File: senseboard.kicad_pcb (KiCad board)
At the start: 6 copper layers, 60 x 100 mm, 81 parts, among them J1 USB_C_Receptacle_USB2.0_16P, J2 Screw_Terminal_01x02, J3 DM3AT-SF-PEJM5, J4 Conn_01x04, J5 Conn_01x08, U1 USBLC6-2SC6, U2 TPS62840DLCR, U3 TPS62840DLCR, U4 SCD41-D-R2, U5 SGP41-D-R4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

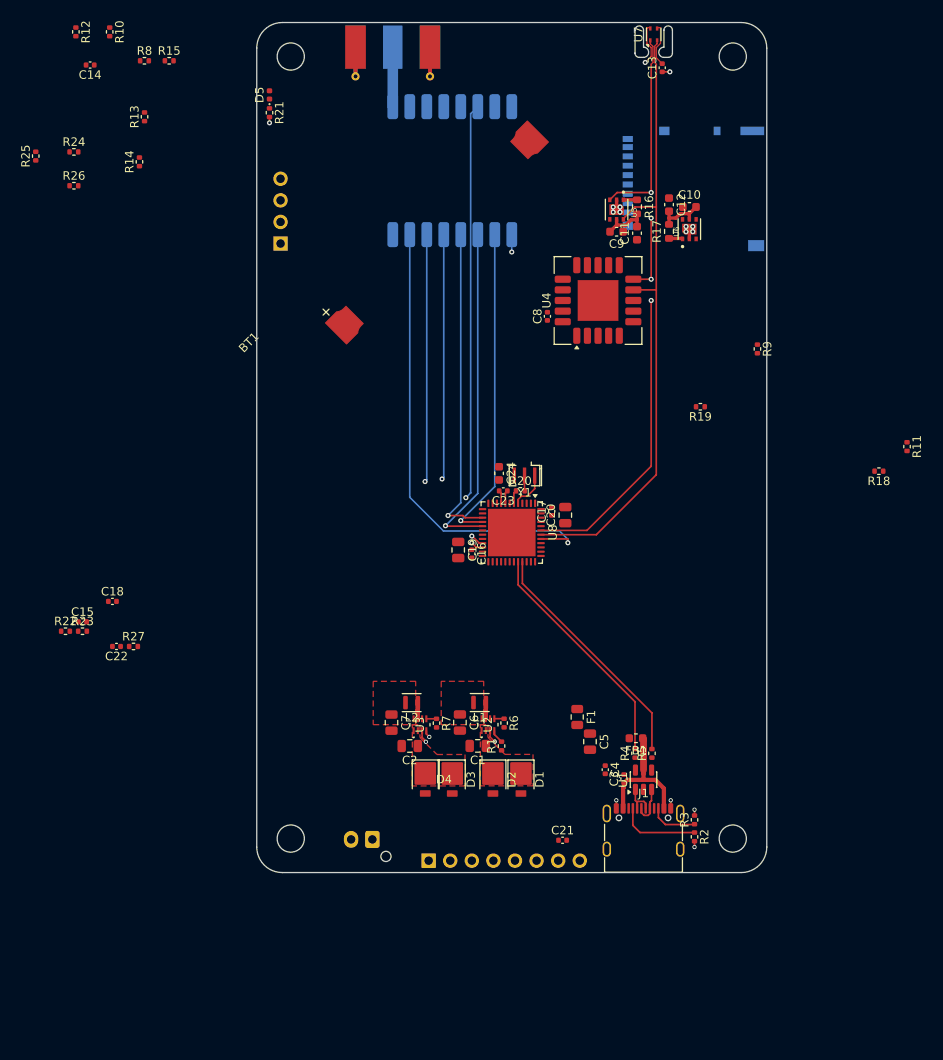
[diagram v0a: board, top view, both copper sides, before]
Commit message: added sd card protection, completed most layout, added bosch sensor, graphics
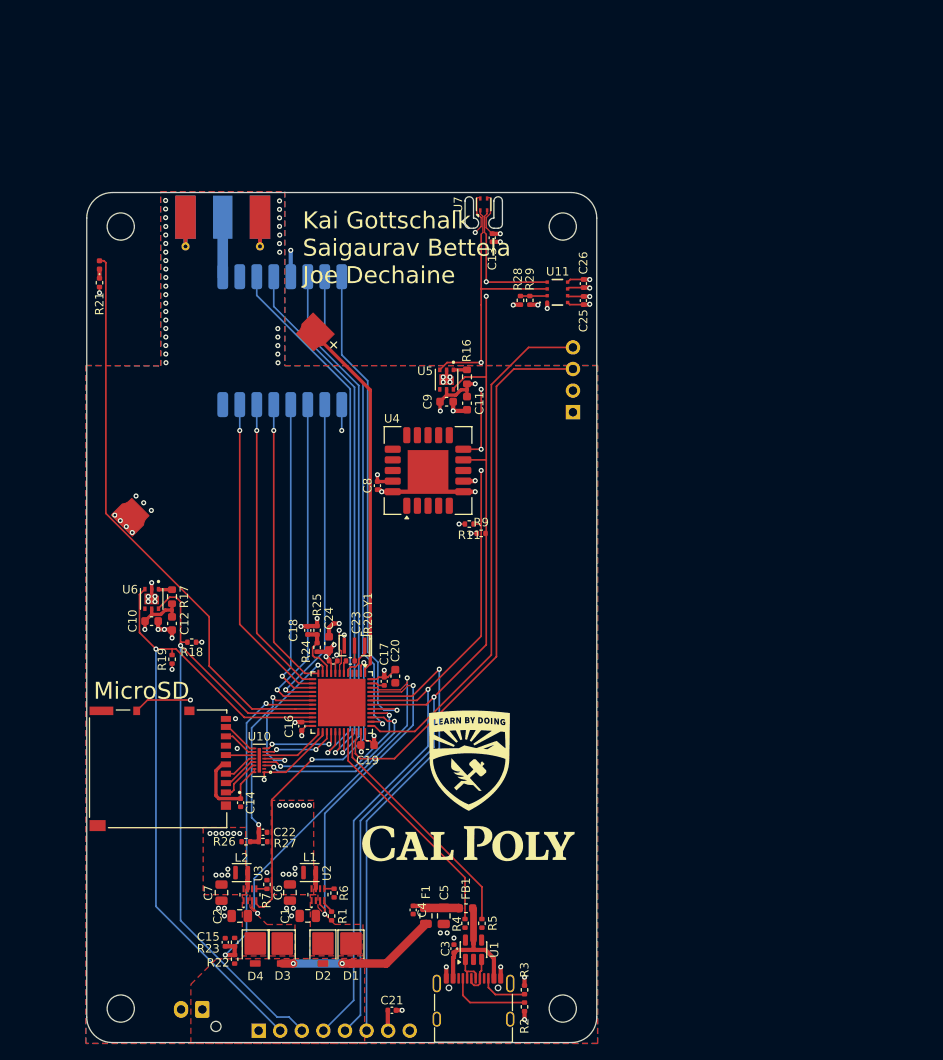
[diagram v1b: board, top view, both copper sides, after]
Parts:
- removed R10, R12, R13, R14, R15, R8: 10k, Resistor_SMD:R_0402_1005Metric
- added C25: 0.1uF, Capacitor_SMD:C_0402_1005Metric, F.Cu at (138.4, 82.7)
- added C26: 0.1uF, Capacitor_SMD:C_0402_1005Metric, F.Cu at (138.4, 80.7)
- added G***: LOGO, graphics:cal_poly_alt-25w, F.Cu at (124.9, 139.8)
- added R28: 0, Resistor_SMD:R_0402_1005Metric, F.Cu at (131.0, 82.7)
- added R29: 0, Resistor_SMD:R_0402_1005Metric, F.Cu at (132.1, 82.7)
- added U10: EMIF06-MSD02N16, EMIF06_MSD02N16:MICROQFN16_1P25X3P55X0P4_STM, F.Cu at (100.3, 136.8)
- added U11: BME690, BME690:BME690, F.Cu at (135.4, 81.7)
- C19, C20: footprint Capacitor_SMD:C_0805_2012Metric -> Capacitor_SMD:C_0603_1608Metric
- J3: moved to F.Cu
- moved J3 93.0 mm to (88.4, 137.8)
- moved C14 88.6 mm to (98.1, 141.8), turned to -90 degrees
- moved R18 83.3 mm to (92.3, 122.9)
- moved C10 79.9 mm to (87.6, 120.4), turned to 180 degrees
- moved R26 79.8 mm to (98.7, 146.4)
- moved U6 76.8 mm to (87.6, 117.8), turned to -90 degrees
- moved C12 76.5 mm to (90.0, 120.7), turned to 90 degrees
- moved R17 72.6 mm to (90.0, 117.5), turned to -90 degrees
- moved R19 68.9 mm to (90.0, 124.9), turned to 90 degrees
- moved R24 64.9 mm to (107.1, 123.5), turned to 90 degrees
- moved R25 64.9 mm to (107.1, 121.5)
- moved R11 52.3 mm to (125.0, 109.0), turned to 0 degrees
- moved R22 43.4 mm to (97.4, 160.2), turned to 90 degrees
- moved C15 41.3 mm to (96.3, 158.2), turned to 90 degrees
- moved R23 40.7 mm to (97.4, 158.2), turned to 90 degrees
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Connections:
- J3 pad 1: /SDMMC_D2 -> /SD_D2
- J3 pad 2: /SDMMC_D3 -> /SD_D3
- J3 pad 3: /SDMMC_CMD -> /SD_CMD
- J3 pad 5: /SDMMC_CLK -> /SD_CLK
- J3 pad 7: /SDMMC_D0 -> /SD_D0
- J3 pad 8: /SDMMC_D1 -> /SD_D1
- J5 pad 2: /I2C1_SDA -> /I2C2_SDA
- J5 pad 3: /I2C1_SCL -> /I2C2_SCL
- J5 pad 4: /I2C2_SDA -> /I2C1_SDA
- J5 pad 5: /I2C2_SCL -> /I2C1_SCL
- U8 pad 10: /VSENSE_BATT -> /VSENSE_3V3_1
- U8 pad 14: /LORA_DIO0 -> /LORA_DIO5
- U8 pad 19: /VSENSE_3V3_1 -> /VSENSE_BATT
- U8 pad 2: unconnected-(U8-PC13-Pad2) -> /3V3_EN2
- U8 pad 30: /LORA_DIO2 -> /LORA_DIO4
- U8 pad 31: /LORA_DIO1 -> /LORA_DIO0
- U8 pad 38: /LORA_DIO4 -> /LORA_DIO1
- U8 pad 41: /LORA_DIO5 -> /LORA_DIO2
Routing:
- net /I2C2_SDA: track 1.49 -> 81.5 mm
- net /I2C2_SCL: track 1.61 -> 80.2 mm
- net /ERROR_LED: track 0.00 -> 67.6 mm
- net /SWDIO: track 0.00 -> 66.1 mm
- net /LORA_DIO3: track 0.00 -> 64.5 mm, vias 0 -> 1
- net /LORA_DIO4: track 0.00 -> 63.5 mm, vias 0 -> 1
- net /SWCLK: track 0.00 -> 61.4 mm
- net /LORA_DIO2: track 0.00 -> 57.7 mm, vias 0 -> 1
- net /RESET: track 0.00 -> 57.3 mm, vias 0 -> 1
- net /LORA_DIO1: track 0.00 -> 56.9 mm, vias 0 -> 1
- net /GPIO_EX: track 0.00 -> 55.4 mm, vias 0 -> 1
- net /I2C1_SDA: track 73.7 -> 127.6 mm, vias 4 -> 5
- net /I2C1_SCL: track 75.0 -> 126.0 mm, vias 0 -> 3
- net Net-(BT1-+): track 0.00 -> 43.8 mm
- net GND: track 15.8 -> 57.4 mm, vias 16 -> 86
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- added copper zone on F.Cu, net +BATT
- added copper zone on B.Cu, net GND
- added copper zone on F.Cu, net GND
- added copper zone on F.Cu, net Net-(D3-K)
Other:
- outline, holes or cut-outs redrawn
- rule pad_to_mask_clearance: 0 -> 0.09
- board text added: "3.8-6.5V"
- board text added: "Designed in SLO, CA"
- board text added: "Kai Gottschalk Saigaurav Bettela Joe Dechaine"
- board text added: "Layout by Kai Gottschalk"
- board text added: "MicroSD"

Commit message: connected n/a on sgp41 to gnd
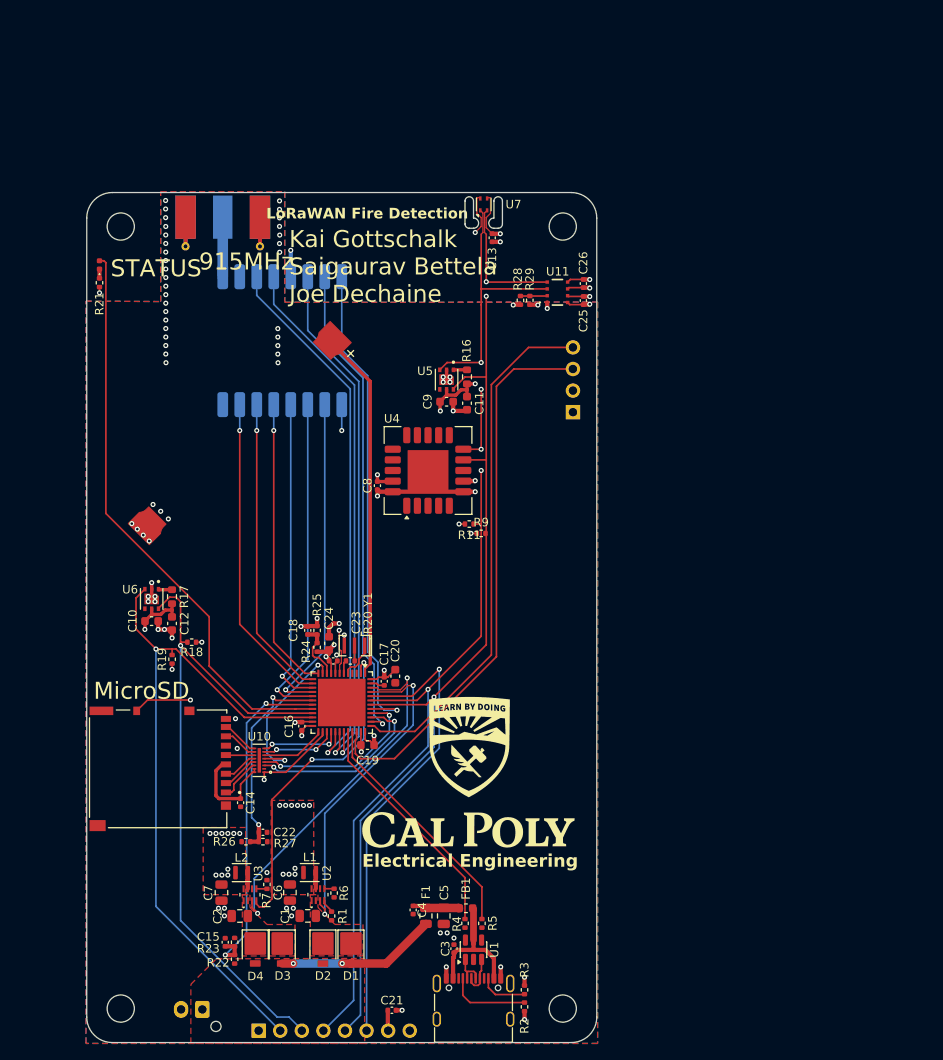
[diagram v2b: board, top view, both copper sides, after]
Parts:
- moved BT1 2.24 mm to (98.0, 98.3)
- moved G*** 1.60 mm to (124.9, 138.2)
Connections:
- U5 pad 4: unconnected-(U5-N/A-Pad4) -> GND
- U6 pad 4: unconnected-(U6-N/A-Pad4) -> GND
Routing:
- net Net-(BT1-+): track 43.8 -> 41.2 mm
- net GND: track 57.4 -> 58.1 mm
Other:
- board text added: "3.9V-6.5V"
- board text added: "3V3"
- board text added: "915MHz"
- board text added: "CLK"
- board text added: "Electrical Engineering"
- board text added: "GND"
- board text added: "IO"
- board text added: "LoRaWAN Fire Detection"
- board text added: "SENSOR STACK"
- board text added: "STATUS"
- board text added: "SWD"
- board text added: "Sensirion SGP41 Sensirion SHT41 Sensirion SCD41 Bosch BME690 RFM95W-915S2R"
- board text added: "USB 2.0"
- board text added: "WIRELESS COMMS"
- board text removed: "3.8-6.5V"

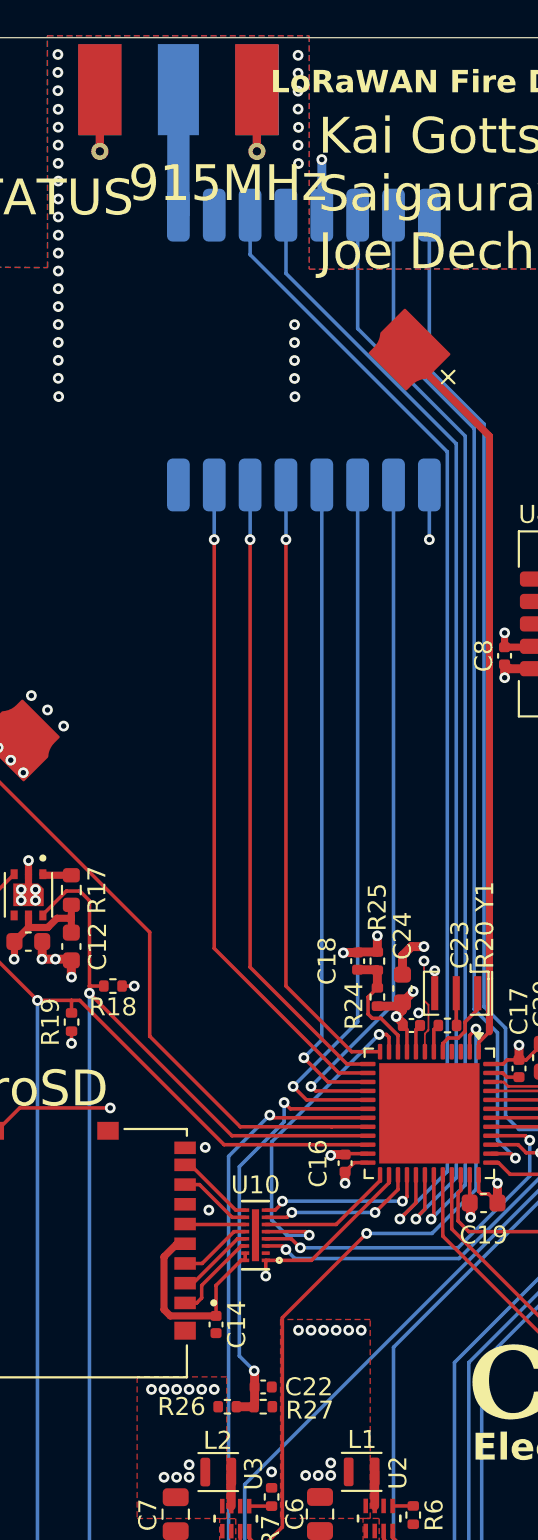
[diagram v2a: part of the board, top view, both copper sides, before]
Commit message: added values and variant for assembly, added 3d model for sd protection to layout, played with via setup
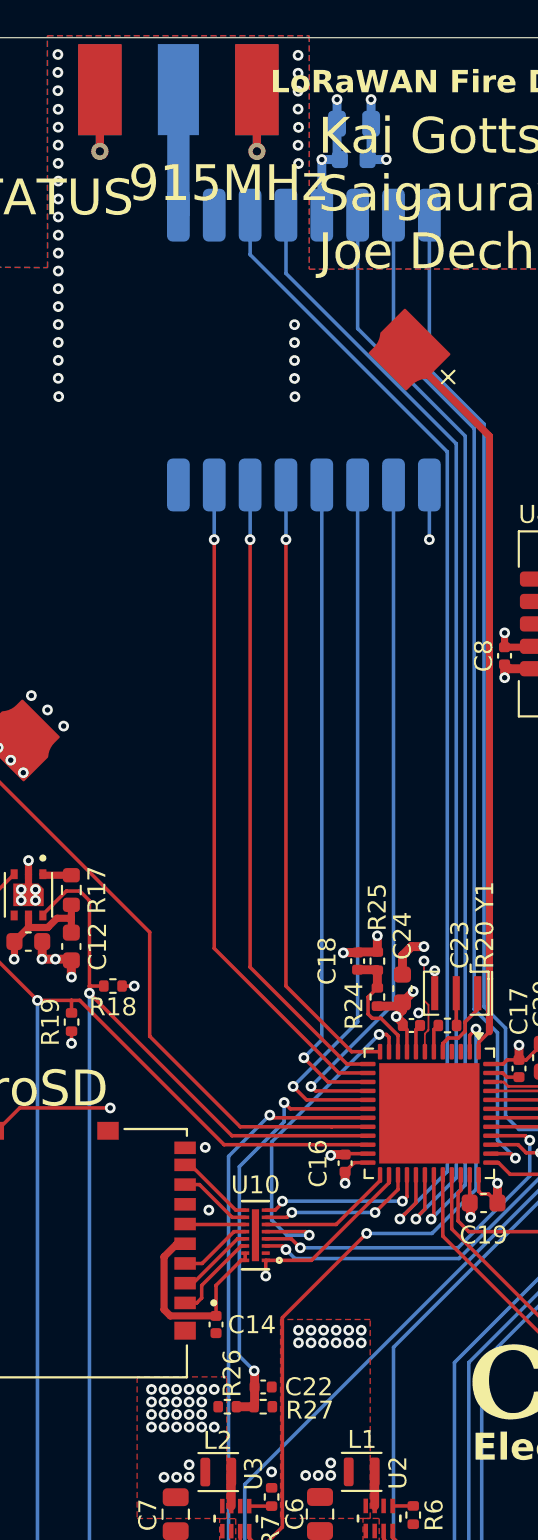
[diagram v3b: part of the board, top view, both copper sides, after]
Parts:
- added C27: 0.1uF, Capacitor_SMD:C_0603_1608Metric, B.Cu at (105.8, 76.8)
- added C28: 1uF, Capacitor_SMD:C_0805_2012Metric, B.Cu at (105.8, 74.8)
- BT1: value Battery_Cell -> CR2032
- R22, R23, R24, R25, R26, R27: value 0 -> 10k
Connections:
- U9 pad 13: +3V3_1 -> +3V3_2
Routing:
- net +3V3_2: track 10.8 -> 18.3 mm, vias 13 -> 31
- net GND: track 58.1 -> 62.6 mm, vias 86 -> 88
- net +3V3_1: track 53.1 -> 50.0 mm, vias 26 -> 31

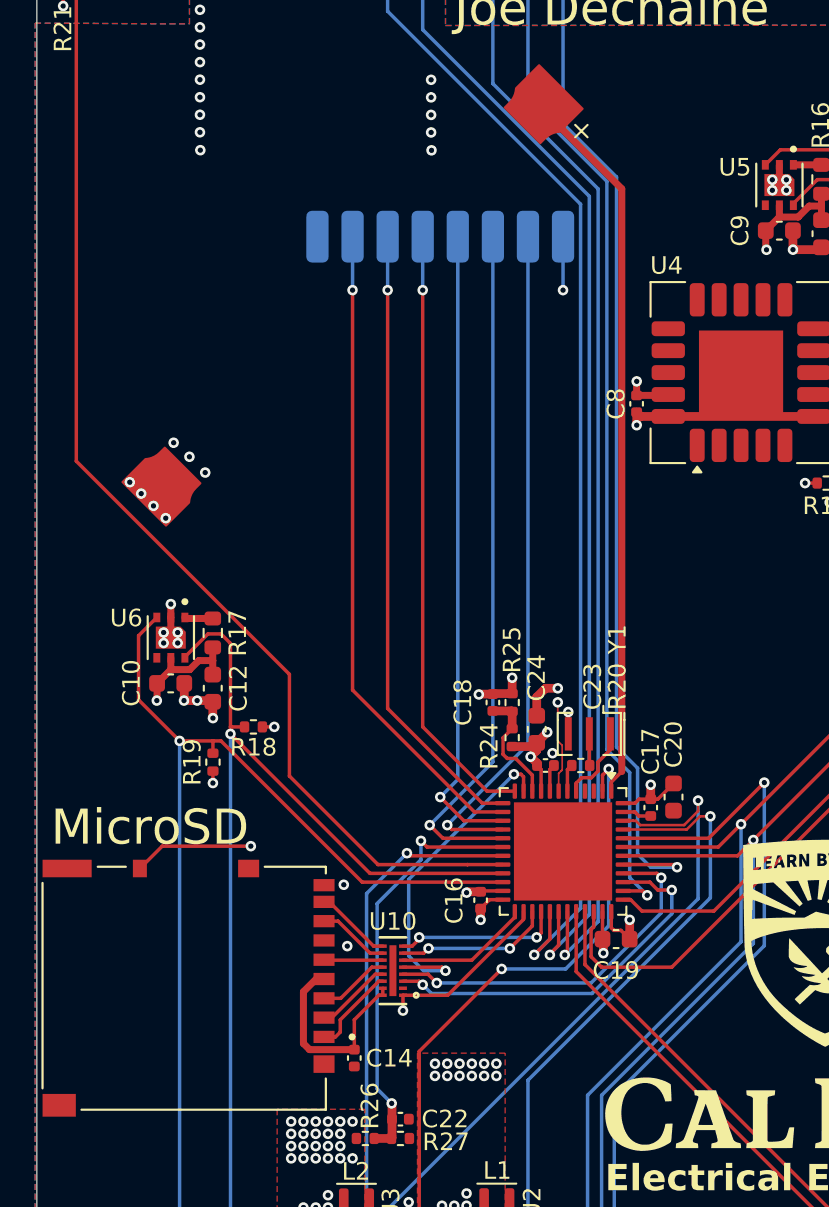
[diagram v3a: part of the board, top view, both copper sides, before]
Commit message: added blocking protection for coin cell and charge limiting
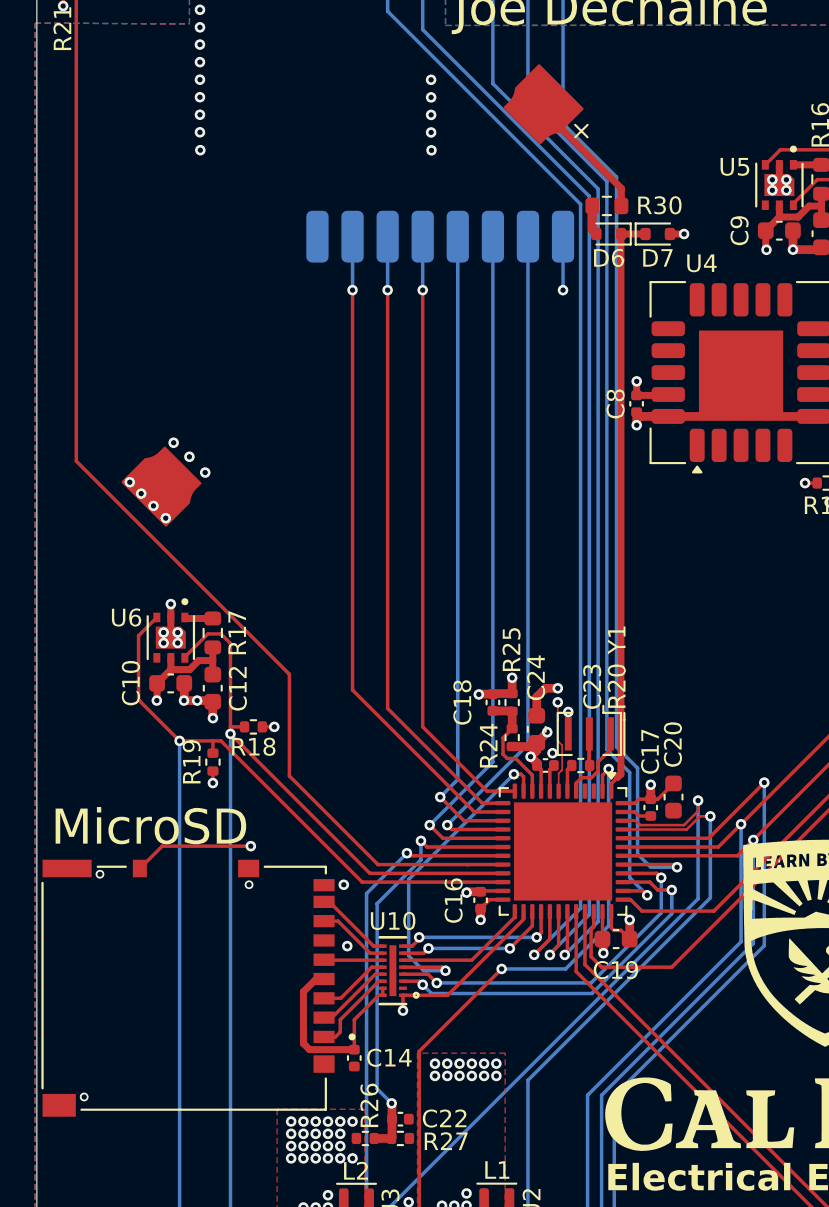
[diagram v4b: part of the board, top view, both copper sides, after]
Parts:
- added D6: D_Schottky, Diode_SMD:D_SOD-523, F.Cu at (112.6, 94.8)
- added D7: D_Schottky, Diode_SMD:D_SOD-523, F.Cu at (115.4, 94.8)
- added R30: 4.7, Resistor_SMD:R_0603_1608Metric, F.Cu at (112.5, 93.2)
- C4: value 100nF -> 0.1uF
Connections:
- U8 pad 1: Net-(BT1-+) -> Net-(D6-K)
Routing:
- net Net-(BT1-+): track 41.2 -> 7.56 mm
- net Net-(D6-K): track 0.00 -> 33.4 mm
- net Net-(D6-A): track 0.00 -> 1.69 mm
- net +3V3_1: track 50.0 -> 50.8 mm, vias 31 -> 32
- net GND: vias 88 -> 91
